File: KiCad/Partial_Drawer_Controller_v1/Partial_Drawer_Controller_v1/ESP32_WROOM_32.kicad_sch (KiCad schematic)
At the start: 37 parts, among them Q1 SS8050, Q2 2N7002T-7-F, Q3 2N7002T-7-F, Q5 SS8050, U6 CP2102N-Axx-xQFN28, U7 ESP32-WROOM-32E-N8, X1 USB-Micro

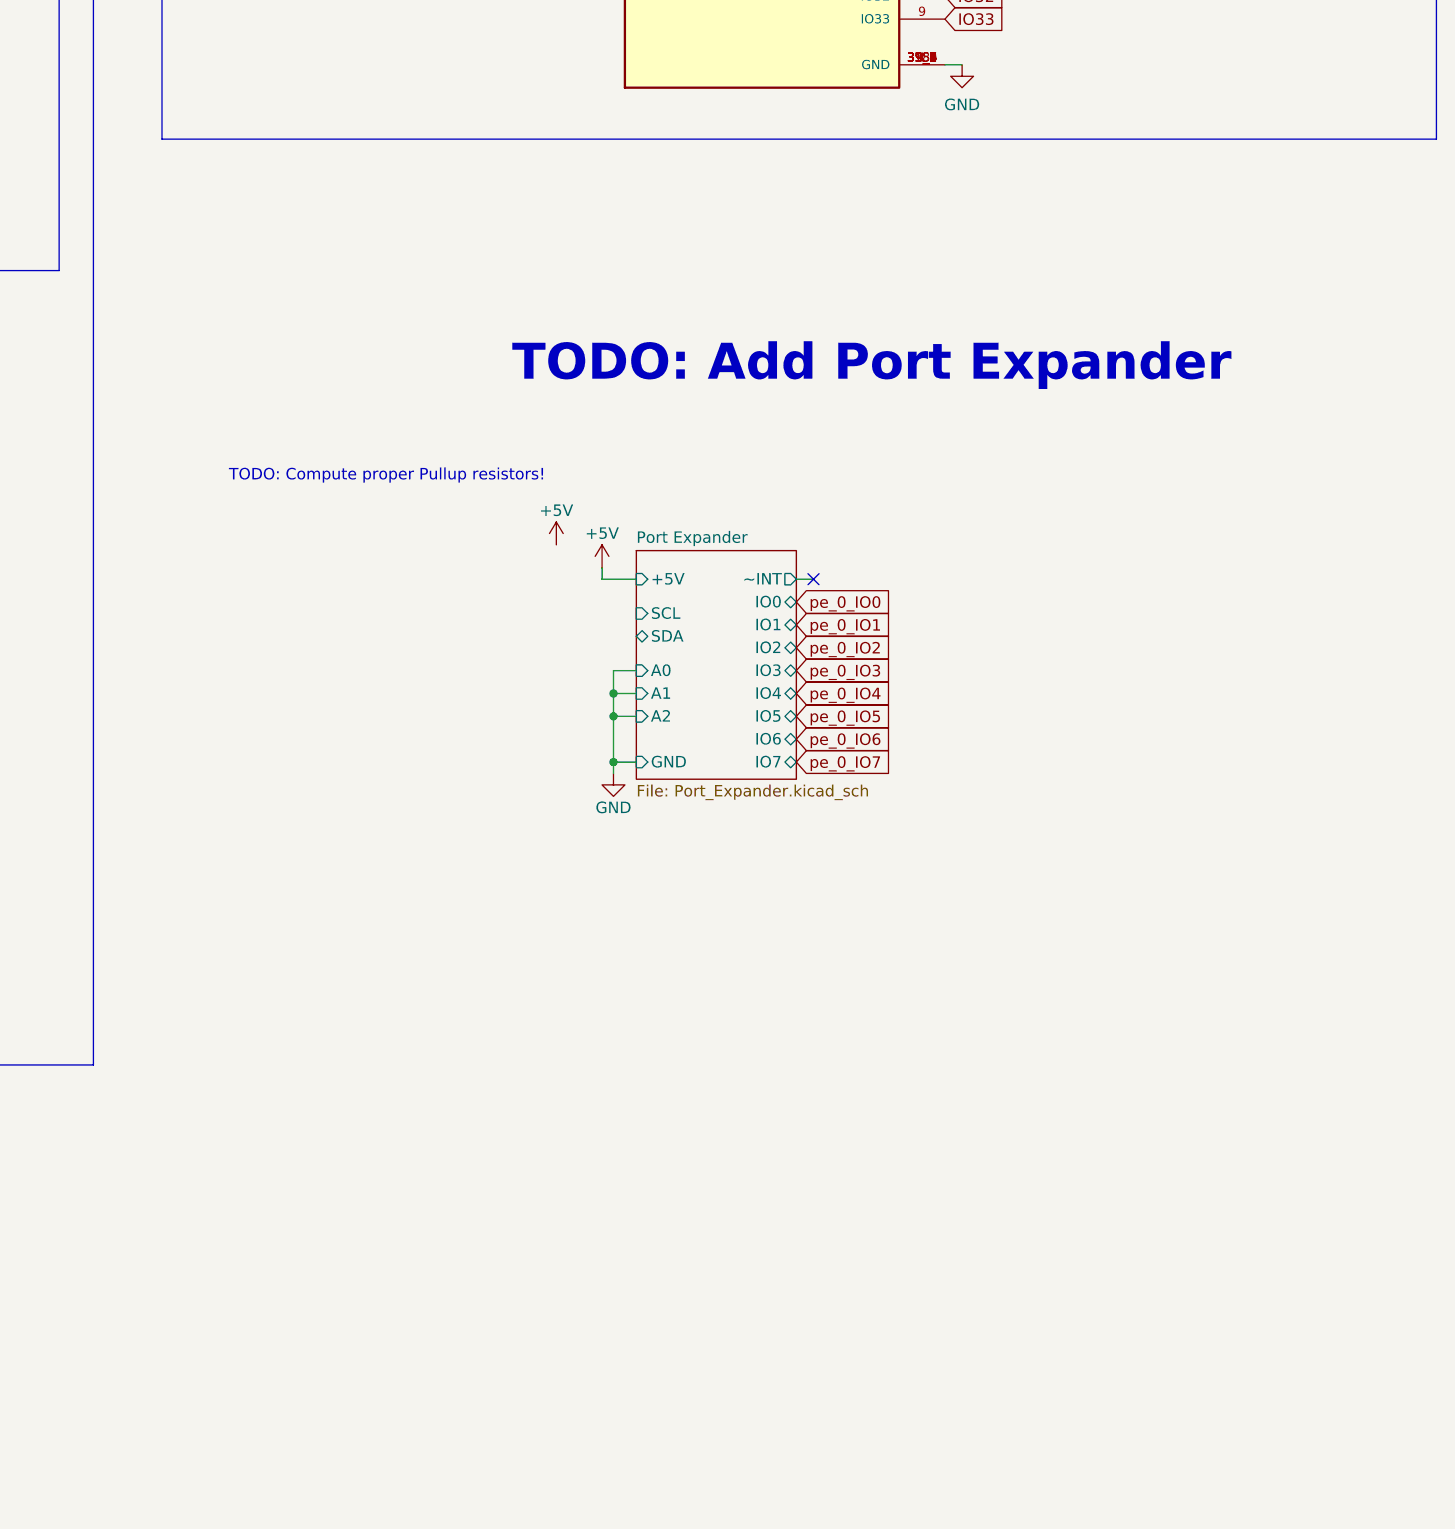
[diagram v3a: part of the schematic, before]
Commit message: feat: finished adding of port expander
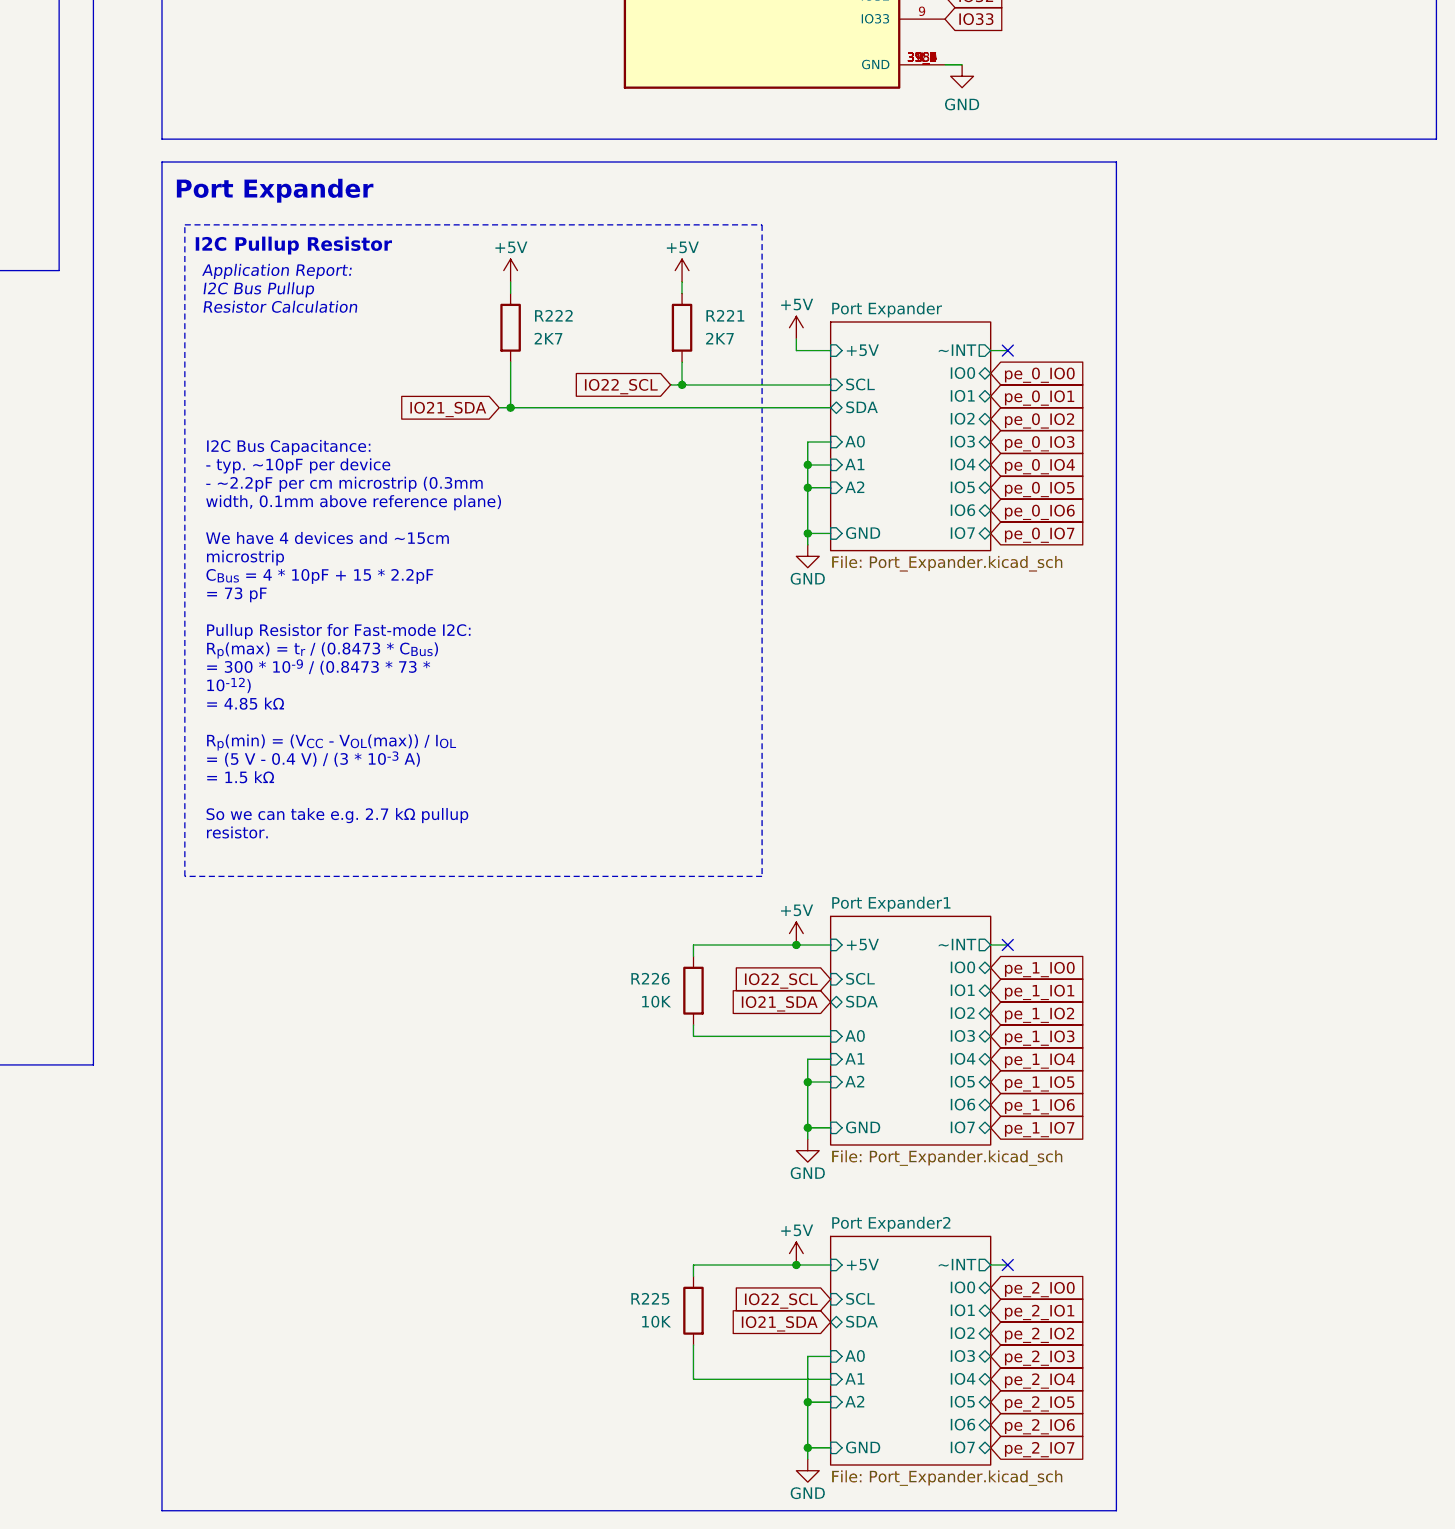
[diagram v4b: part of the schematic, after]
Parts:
- added R221, R222: 2K7, Resistor_SMD:R_0603_1608Metric, symbol _R_0603:2K7
- added R225, R226: 10K, Resistor_SMD:R_0402_1005Metric, symbol _R_0402:10K
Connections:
- net +5V: now also R221.1, R222.1, R225.1, R226.1
- net IO21_SDA: now also R222.2
- net IO22_SCL: now also R221.2
- new net Port Expander1/A0: R226.2
- new net Port Expander2/A1: R225.2
- no-connect marks 19 -> 21
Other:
- added sheet Port Expander1 (Port_Expander.kicad_sch)
- added sheet Port Expander2 (Port_Expander.kicad_sch)
- note added: "Application Report: I2C Bus Pullup Resistor Calculation"
- note added: "I2C Pullup Resistor"
- note added: "Port Expander"
- note removed: "TODO: Add Port Expander"
- note removed: "TODO: Compute proper Pullup resistors!"

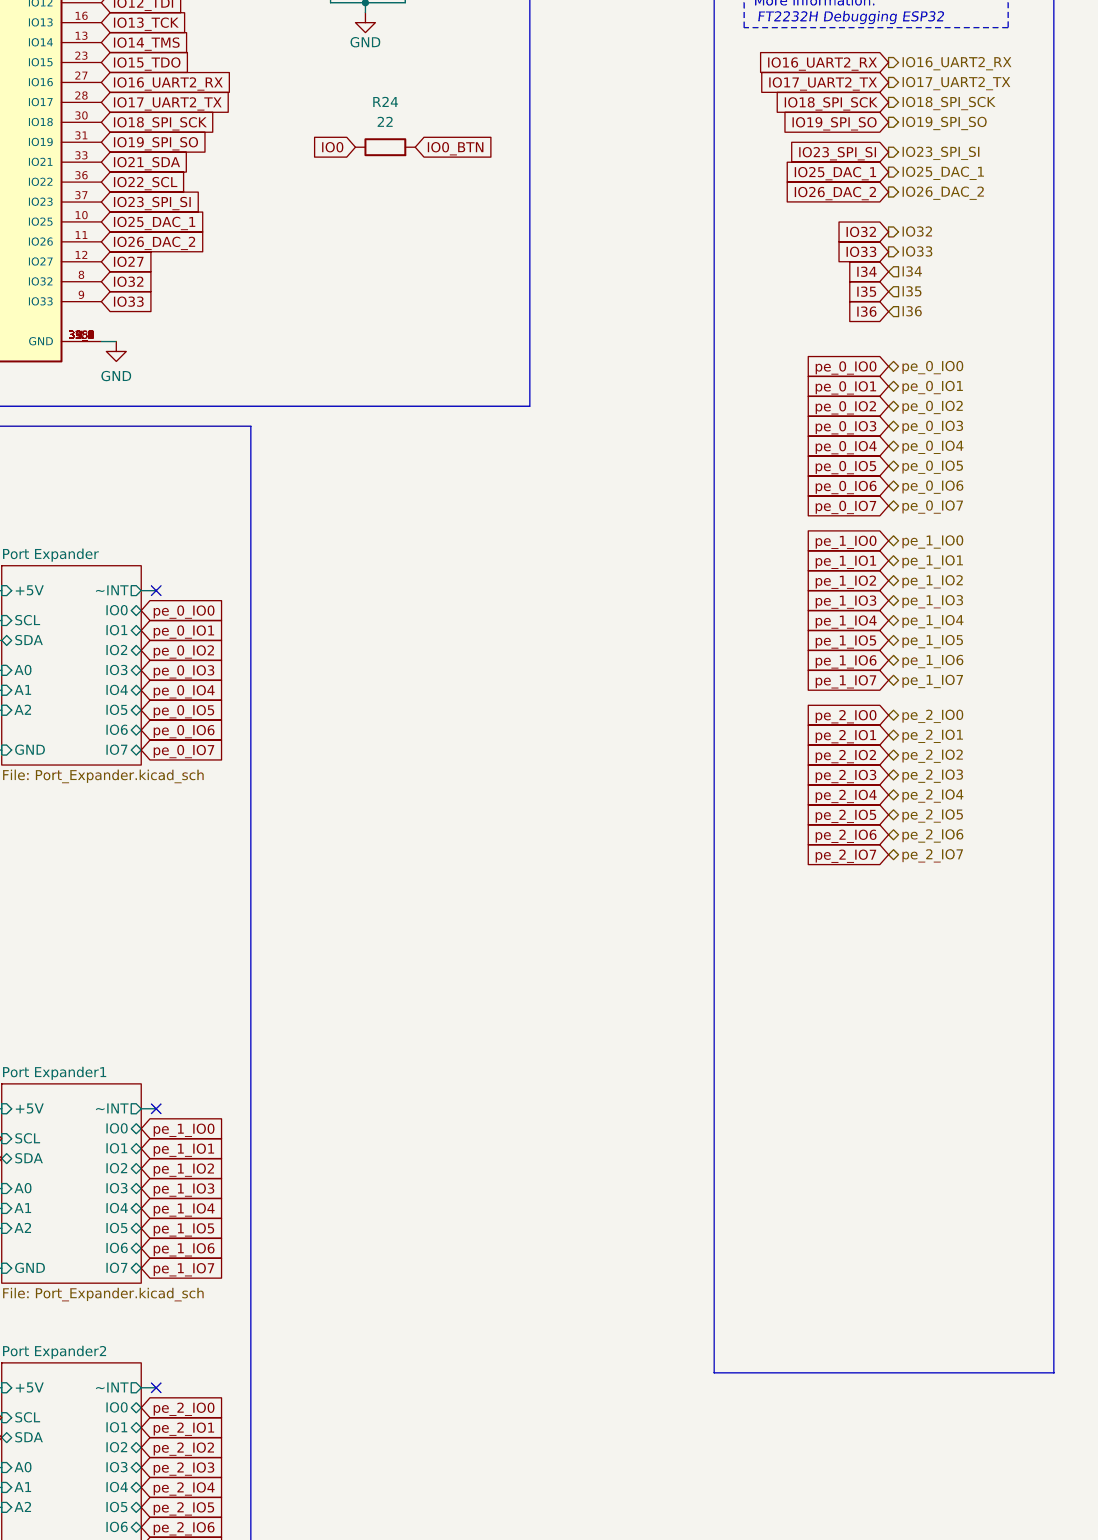
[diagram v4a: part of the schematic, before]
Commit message: feat: first draft for connection esp32 and port expander to stuff on the pcb
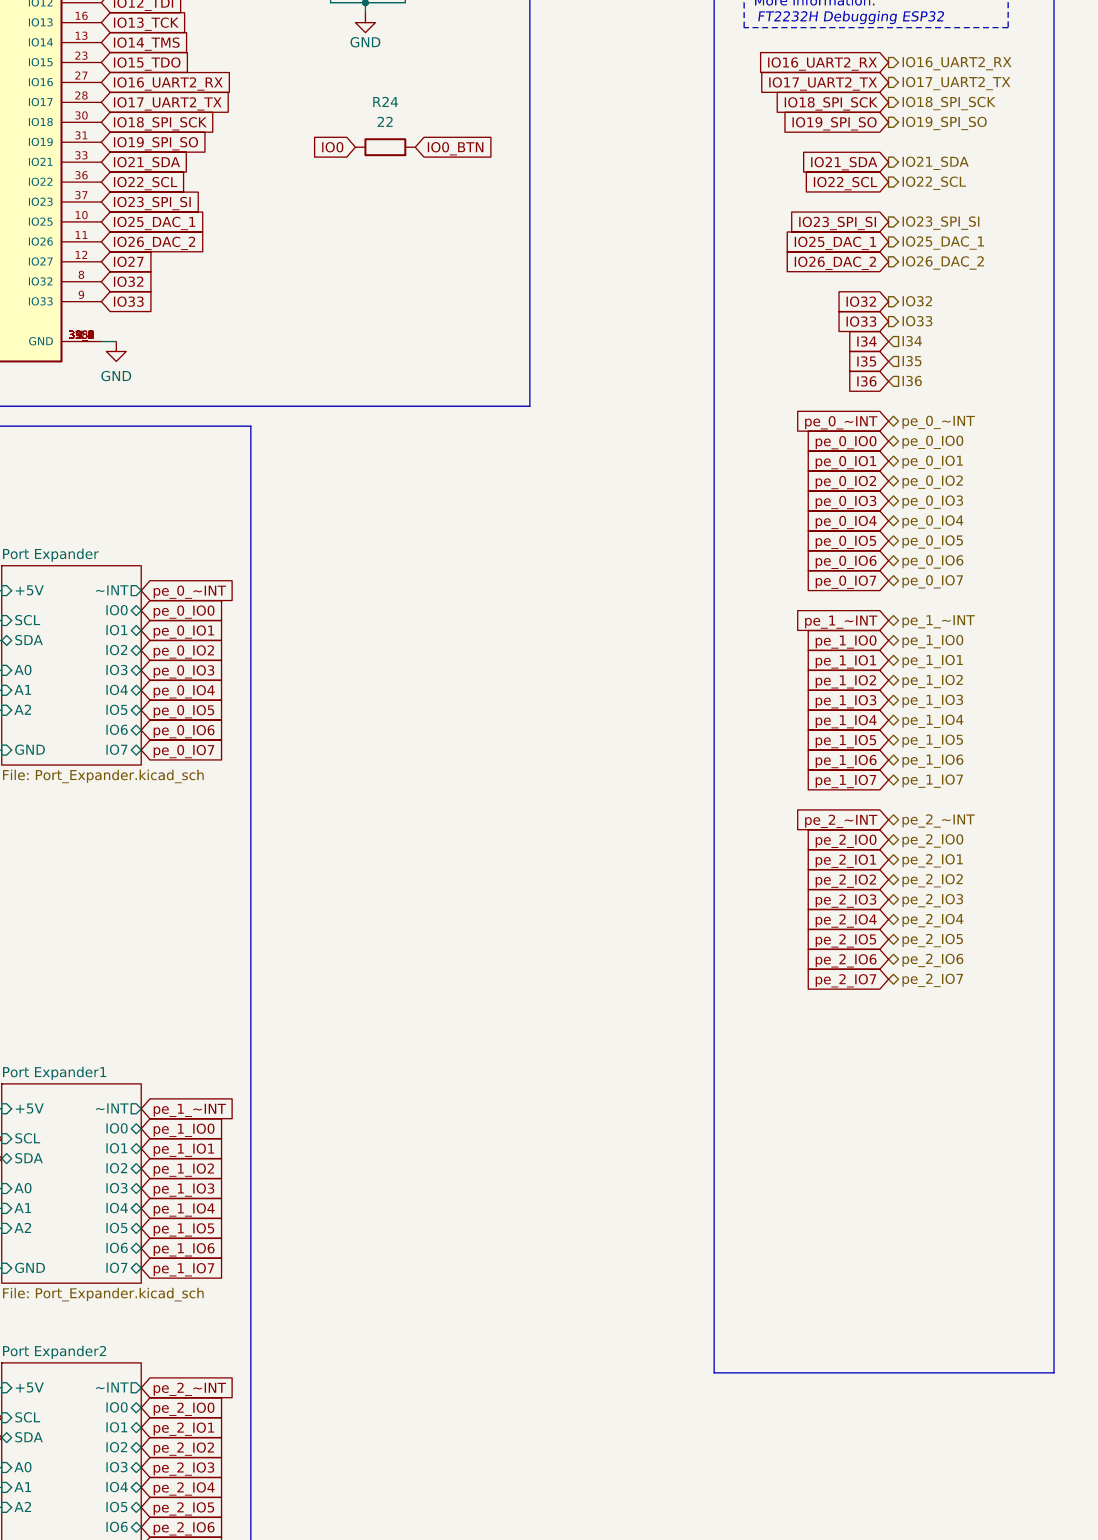
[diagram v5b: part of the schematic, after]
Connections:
- no-connect marks 21 -> 18
